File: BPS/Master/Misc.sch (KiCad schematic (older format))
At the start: 19 parts, among them J3 FrontFans, J4 BackFans, Q6 BUT11

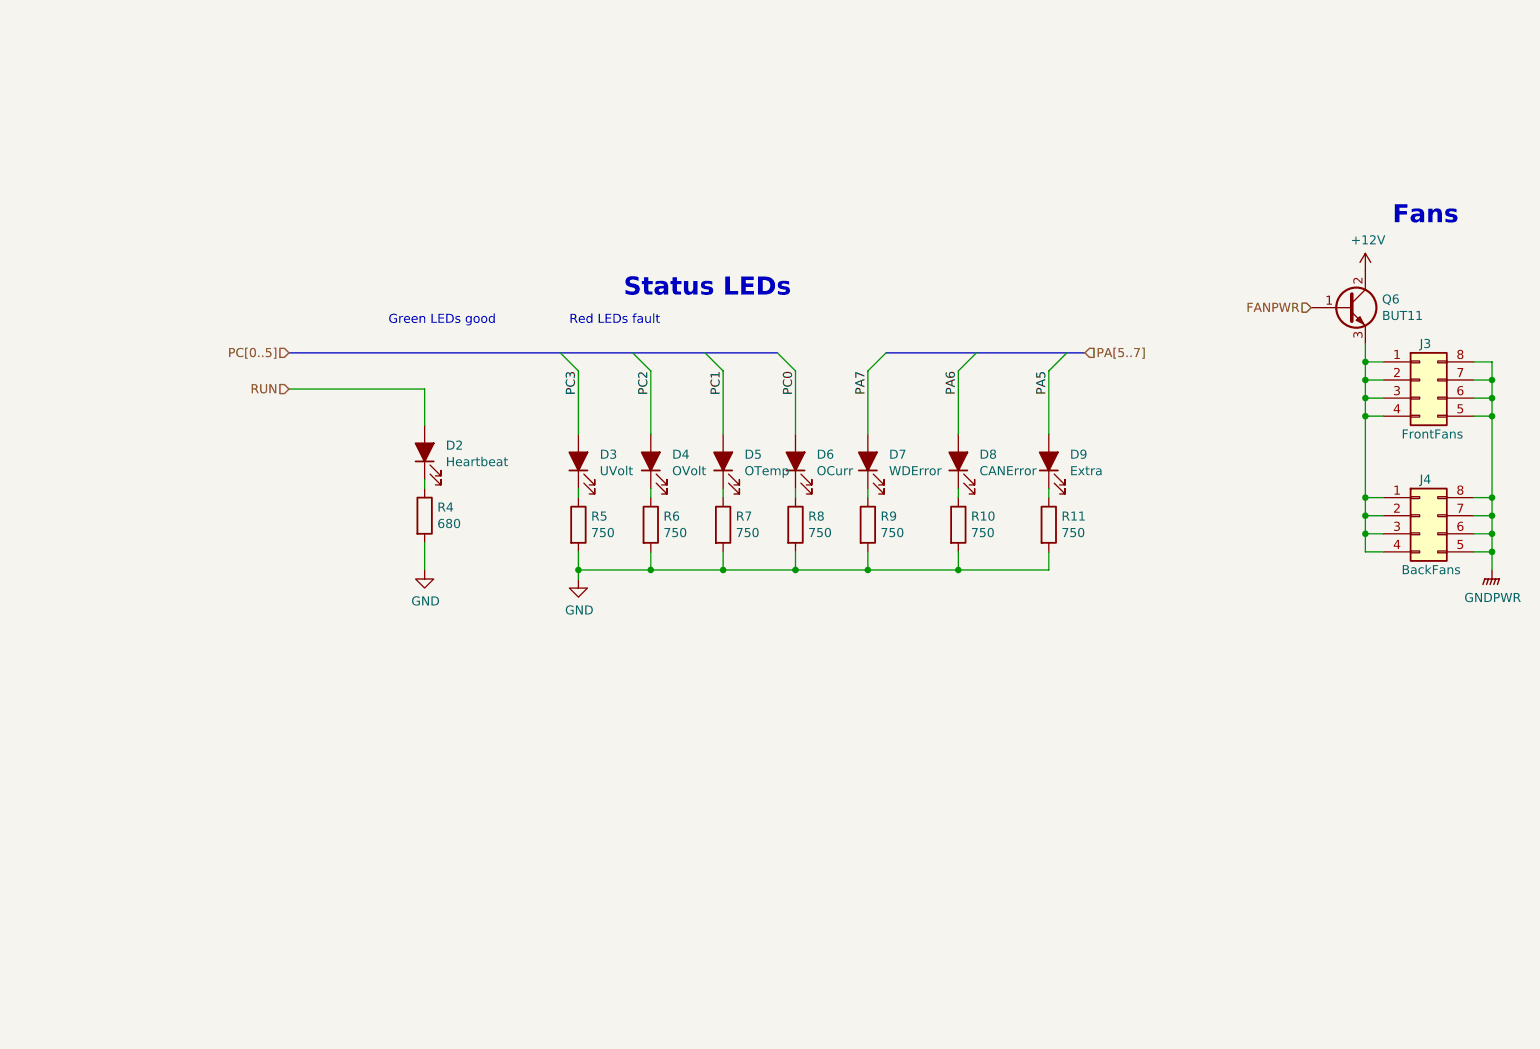
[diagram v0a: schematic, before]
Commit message: Added Interface Pins to Misc sheet so we don't have to make a revision every time we want to add something. Also fixed the input/output for the hierarchial labels.
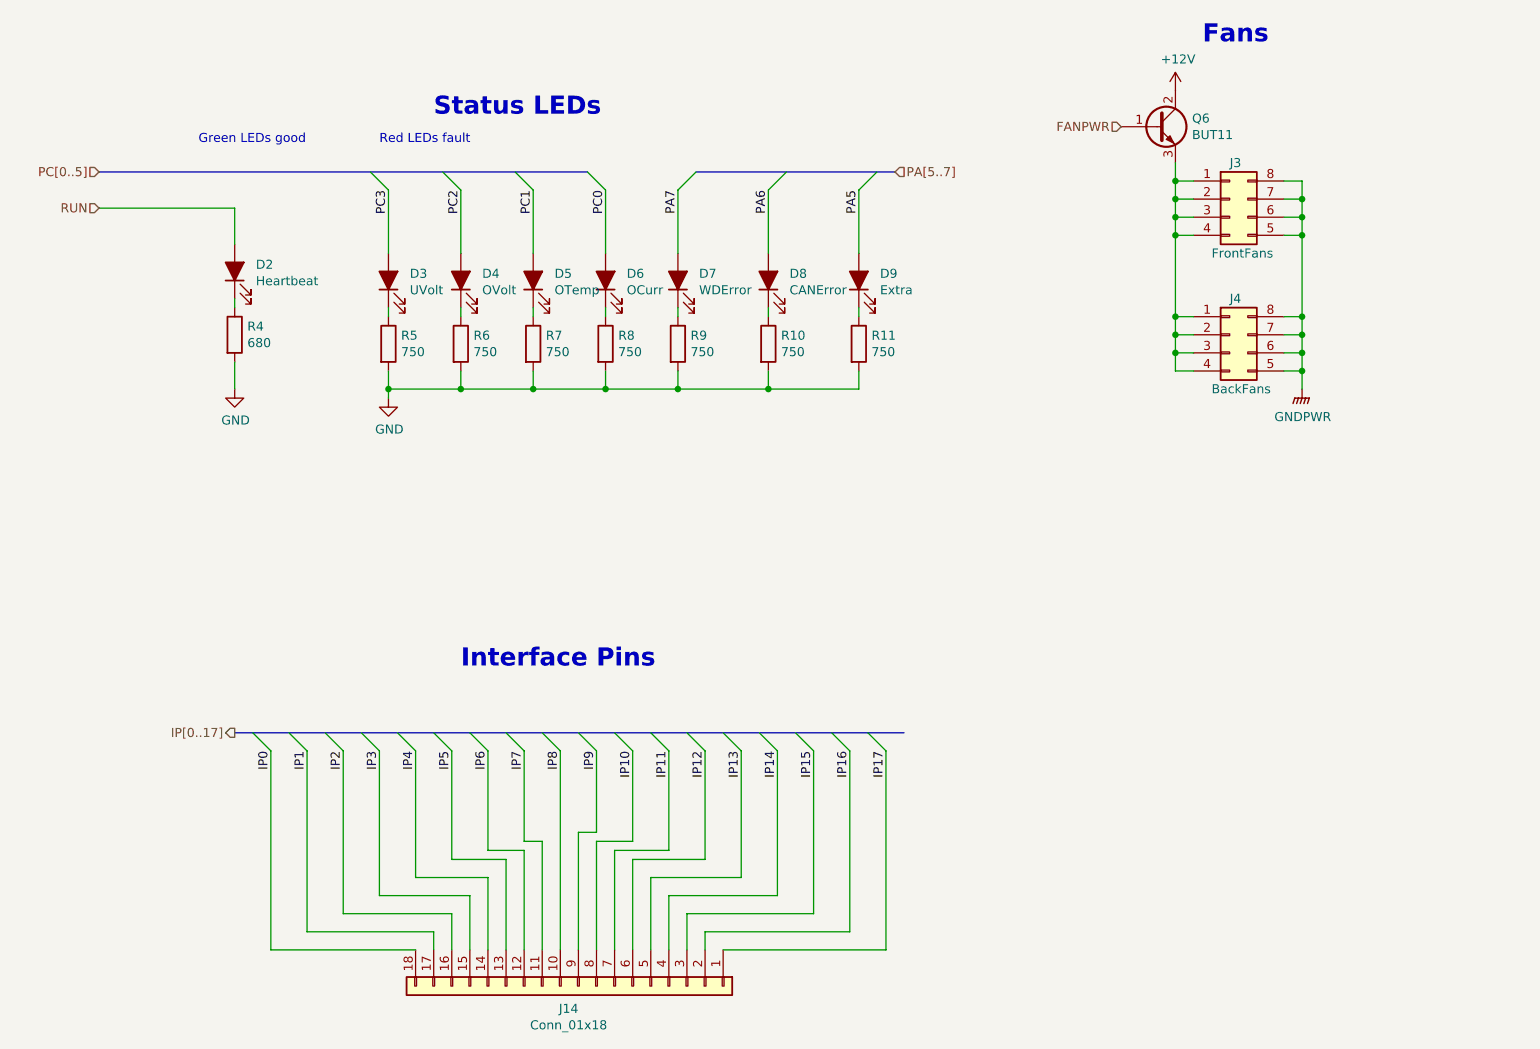
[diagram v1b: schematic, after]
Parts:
- added J14: Conn_01x18, symbol Connector_Generic:Conn_01x18
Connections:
- new net IP0: J14.18 (Pin_18)
- new net IP1: J14.17 (Pin_17)
- new net IP10: J14.8 (Pin_8)
- new net IP11: J14.7 (Pin_7)
- new net IP12: J14.6 (Pin_6)
- new net IP13: J14.5 (Pin_5)
- new net IP14: J14.4 (Pin_4)
- new net IP15: J14.3 (Pin_3)
- new net IP16: J14.2 (Pin_2)
- new net IP17: J14.1 (Pin_1)
- new net IP2: J14.16 (Pin_16)
- new net IP3: J14.15 (Pin_15)
- new net IP4: J14.14 (Pin_14)
- new net IP5: J14.13 (Pin_13)
- new net IP6: J14.12 (Pin_12)
- new net IP7: J14.11 (Pin_11)
- new net IP8: J14.10 (Pin_10)
- new net IP9: J14.9 (Pin_9)
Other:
- note added: "Interface Pins"
- moved on the sheet: D2, D3, D4, D5, D6, D7, D8, D9, J3, J4, Q6, R10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
